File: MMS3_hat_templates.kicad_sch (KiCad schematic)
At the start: 12 parts, among them U4 AMS1117

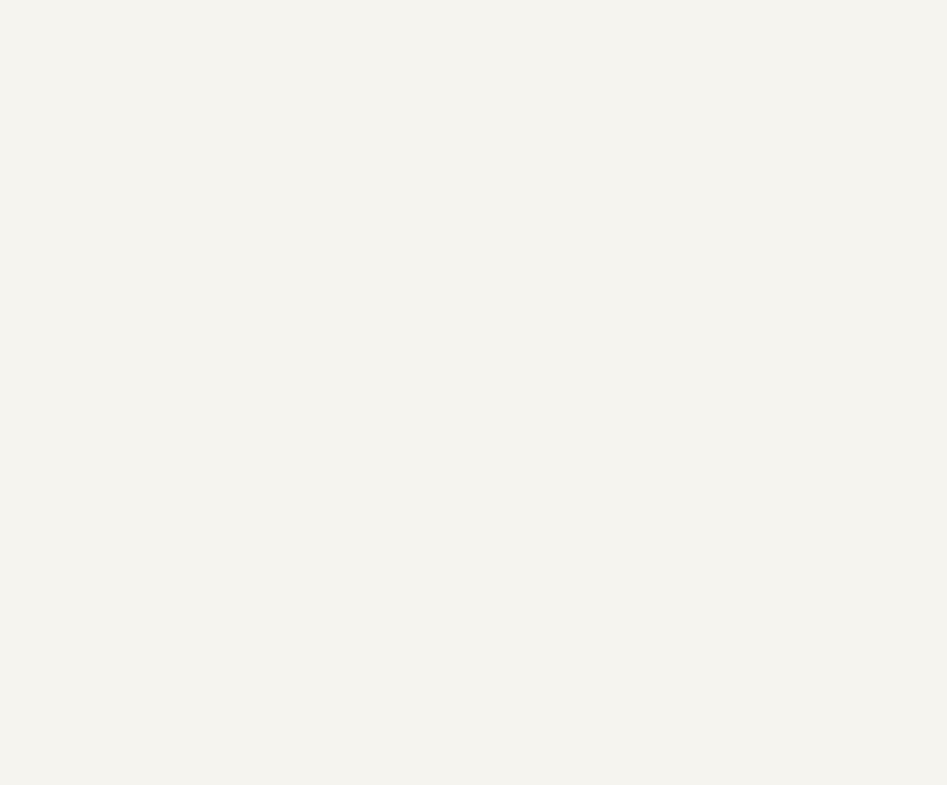
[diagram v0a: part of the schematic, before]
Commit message: Dodałem przetworkę
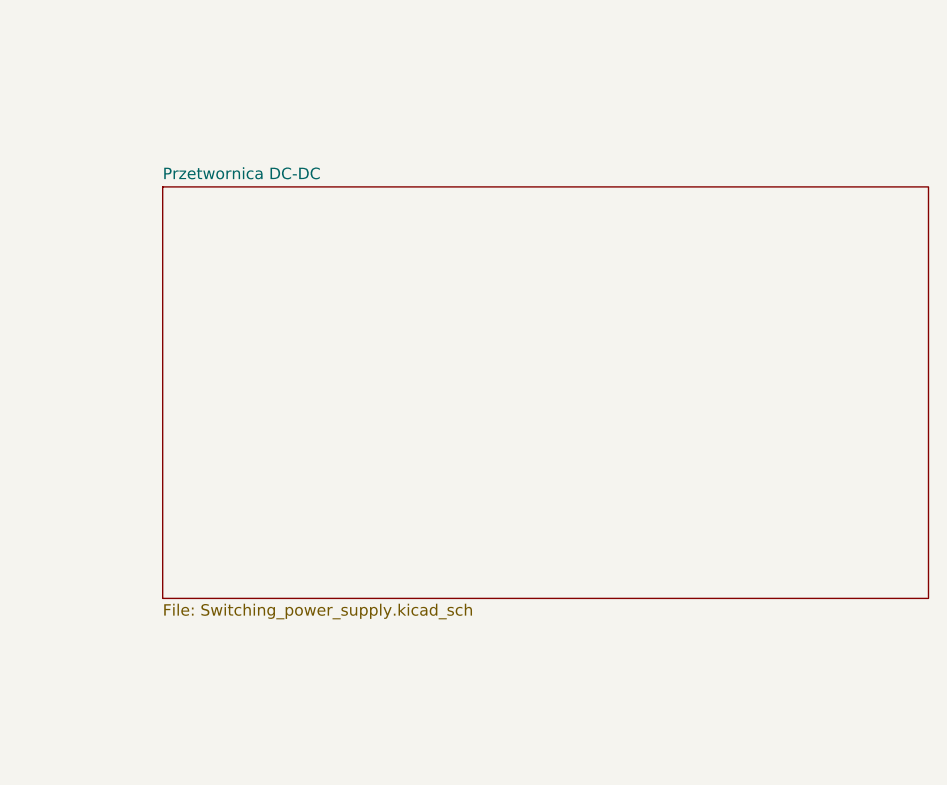
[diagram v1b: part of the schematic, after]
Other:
- added sheet Przetwornica DC-DC (Switching_power_supply.kicad_sch)
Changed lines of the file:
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@@
+	)
+	(sheet
+		(at 129.54 41.91)
+		(size 85.09 45.72)
+		(exclude_from_sim no)
+		(in_bom yes)
+		(on_board yes)
+		(dnp no)
+		(fields_autoplaced yes)
+		(stroke
+			(width 0.1524)
+			(type solid)
+		)
+		(fill
+			(color 0 0 0 0)
+		)
+		(property "Sheetname" "Przetwornica DC-DC"
+			(at 129.54 41.1984 0)
+			(show_name no)
+			(do_not_autoplace no)
+			(effects
+				(font
+					(size 1.27 1.27)
+				)
+				(justify left bottom)
+			)
+		)
+		(property "Sheetfile" "Switching_power_supply.kicad_sch"
+			(at 129.54 88.2146 0)
+			(show_name no)
+			(do_not_autoplace no)
+			(effects
+				(font
+					(size 1.27 1.27)
+				)
+				(justify left top)
+			)
+		)
+		(instances
+			(project "MMS3_hat_templates"
+				(path "/6596548a-44e0-46d8-8624-fd71cf4a3e17"
+					(page "6")
+				)
+			)
+		)
 	)
 	(sheet

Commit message: moved sth and added hierarhical pins
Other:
- sheet Przetwornica DC-DC ports: added VIN, VOUT; removed none
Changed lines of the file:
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@@
 		)
 	)
+	(wire
+		(pts
+			(xy 52.07 130.81) (xy 78.74 130.81)
+		)
+		(stroke
+			(width 0)
+			(type default)
+		)
+	)
 	(bus
 		(pts
@@
 	)
 	(sheet
-		(at 129.54 41.91)
-		(size 85.09 45.72)
+		(at 78.74 122.555)
+		(size 31.75 25.4)
 		(exclude_from_sim no)
 		(in_bom yes)
@@
 		)
 		(property "Sheetname" "Przetwornica DC-DC"
-			(at 129.54 41.1984 0)
+			(at 78.74 121.8434 0)
 			(show_name no)
 			(do_not_autoplace no)
@@
 		)
 		(property "Sheetfile" "Switching_power_supply.kicad_sch"
-			(at 129.54 88.2146 0)
+			(at 78.74 148.5396 0)
 			(show_name no)
 			(do_not_autoplace no)
@@
 			)
 		)
+		(pin "VIN" input
+			(at 78.74 130.81 180)
+			(effects
+				(font
+					(size 1.27 1.27)
+				)
+				(justify left)
+			)
+		)
+		(pin "VOUT" input
+			(at 110.49 130.81 0)
+			(effects
+				(font
+					(size 1.27 1.27)
+				)
+				(justify right)
+			)
+		)
